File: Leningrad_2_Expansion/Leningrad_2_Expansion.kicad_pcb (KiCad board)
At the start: 2 copper layers, 40 x 71 mm, 2 parts, among them J1 ZX_Spectrum_Connector_48K, X6 Leningrad 2 Expansion Bus

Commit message: PCB changes
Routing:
- net GND: track 136.5 -> 119.8 mm, vias 24 -> 32
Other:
- board text added: "28A"
- board text added: "4A"
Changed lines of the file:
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@@
+		)
+	)
+	(gr_text "4A"
+		(at 77.599998 31.878654 0)
+		(layer "F.SilkS")
+		(effects
+			(font
+				(size 1 1)
+				(thickness 0.1)
+			)
+			(justify left bottom)
 		)
 	)
@@
 		)
 	)
+	(gr_text "28A"
+		(at 77.599998 92.578654 0)
+		(layer "F.SilkS")
+		(effects
+			(font
+				(size 1 1)
+				(thickness 0.1)
+			)
+			(justify left bottom)
+		)
+	)
 	(gr_text "21A (~{WAIT})"
 		(at 77.599998 75.057308 0)
@@
 		(layer "B.Cu")
 		(net 14)
-	)
-	(segment
-		(start 76.849998 62.007308)
-		(end 78.799998 63.957308)
-		(width 0.5)
-		(layer "F.Cu")
-		(net 15)
 	)
 	(segment
@@
 	)
 	(segment
-		(start 73.799998 50.74073)
-		(end 73.799998 51.457308)
+		(start 66.199999 48.178654)
+		(end 66.599999 48.578654)
 		(width 0.5)
 		(layer "F.Cu")
@@
 	)
 	(segment
-		(start 78.38342 46.157308)
-		(end 73.799998 50.74073)
-		(width 0.5)
-		(layer "F.Cu")
-		(net 15)
-	)
-	(segment
-		(start 65.099998 68.057308)
-		(end 65.099998 65.657308)
-		(width 0.5)
-		(layer "F.Cu")
-		(net 15)
-	)
-	(segment
-		(start 80.399998 49.857308)
-		(end 85.299998 49.857308)
-		(width 0.5)
-		(layer "F.Cu")
-		(net 15)
-	)
-	(segment
 		(start 78.099998 71.257308)
 		(end 80.099998 73.257308)
@@
 	)
 	(segment
-		(start 85.299998 49.857308)
-		(end 85.399998 49.957308)
-		(width 0.5)
-		(layer "F.Cu")
-		(net 15)
-	)
-	(segment
-		(start 80.499998 46.157308)
-		(end 78.38342 46.157308)
-		(width 0.5)
-		(layer "F.Cu")
-		(net 15)
-	)
-	(segment
-		(start 75.299998 60.457308)
-		(end 76.849998 62.007308)
-		(width 0.5)
-		(layer "F.Cu")
-		(net 15)
-	)
-	(segment
-		(start 78.799998 63.957308)
-		(end 80.499998 63.957308)
+		(start 60.099999 48.178654)
+		(end 66.199999 48.178654)
 		(width 0.5)
 		(layer "F.Cu")
@@
 	)
 	(via
+		(at 56.299999 23.978654)
+		(size 0.6)
+		(drill 0.3)
+		(layers "F.Cu" "B.Cu")
+		(free yes)
+		(net 15)
+	)
+	(via
+		(at 73.099999 45.278654)
+		(size 0.6)
+		(drill 0.3)
+		(layers "F.Cu" "B.Cu")
+		(free yes)
+		(net 15)
+	)
+	(via
 		(at 83.899998 78.157308)
 		(size 0.6)
@@
 	)
 	(via
+		(at 75.299999 64.878654)
+		(size 0.6)
+		(drill 0.3)
+		(layers "F.Cu" "B.Cu")
+		(free yes)
+		(net 15)
+	)
+	(via
 		(at 68.199998 80.757308)
 		(size 0.6)
@@
 	)
 	(via
+		(at 64.099999 60.878654)
+		(size 0.6)
+		(drill 0.3)
+		(layers "F.Cu" "B.Cu")
+		(free yes)
+		(net 15)
+	)
+	(via
 		(at 75.299998 60.457308)
 		(size 0.6)
@@
 	)
 	(via
+		(at 66.599999 48.578654)
+		(size 0.6)
+		(drill 0.3)
+		(layers "F.Cu" "B.Cu")
+		(net 15)
+	)
+	(via
 		(at 73.799998 51.457308)
 		(size 0.6)
@@
 	)
 	(via
+		(at 66.699999 44.278654)
+		(size 0.6)
+		(drill 0.3)
+		(layers "F.Cu" "B.Cu")
+		(free yes)
+		(net 15)
+	)
+	(via
+		(at 68.899999 53.878654)
+		(size 0.6)
+		(drill 0.3)
+		(layers "F.Cu" "B.Cu")
+		(free yes)
+		(net 15)
+	)
+	(via
 		(at 80.499998 63.957308)
 		(size 0.6)
@@
 		(net 15)
 	)
+	(via
+		(at 66.499999 39.978654)
+		(size 0.6)
+		(drill 0.3)
+		(layers "F.Cu" "B.Cu")
+		(free yes)
+		(net 15)
+	)

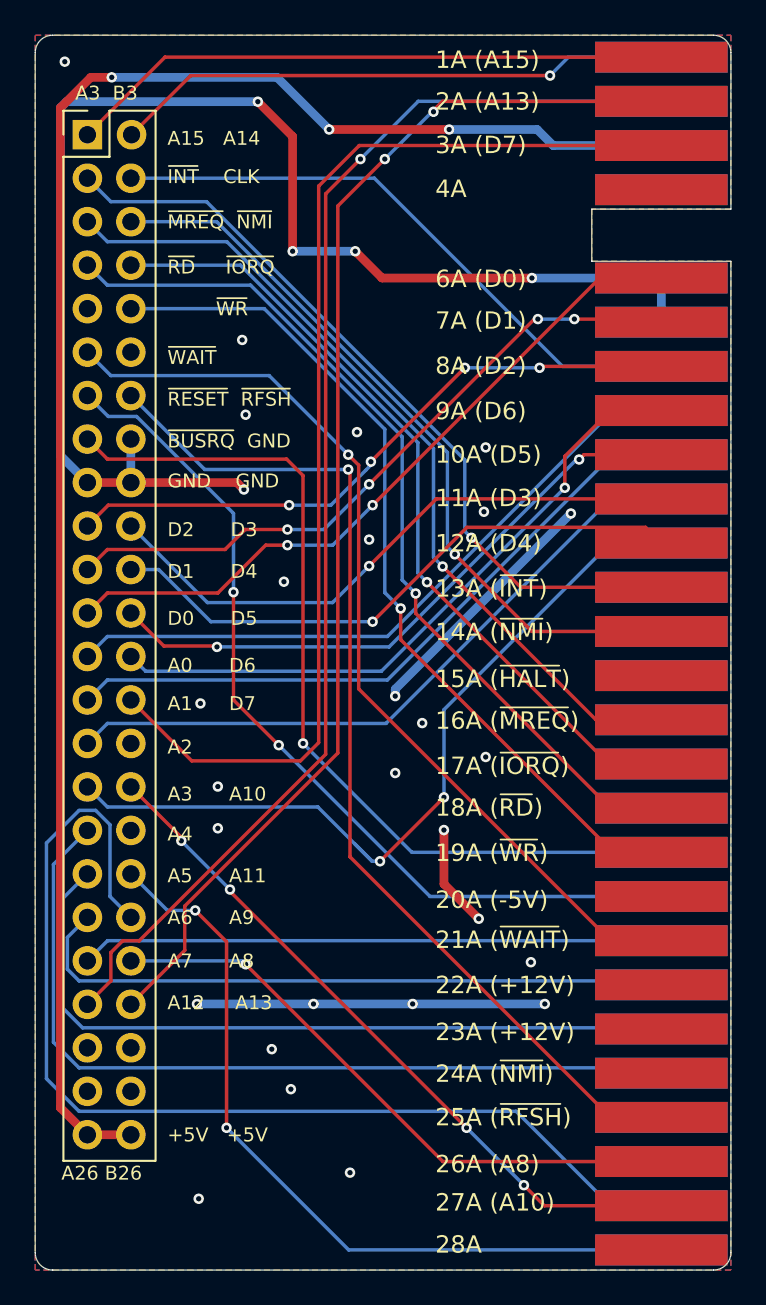
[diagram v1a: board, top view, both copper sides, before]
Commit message: Added ~IORQGE signal
Thanks to Oleh S. suggestion on UCHC "Ukrainian Computing History Community"
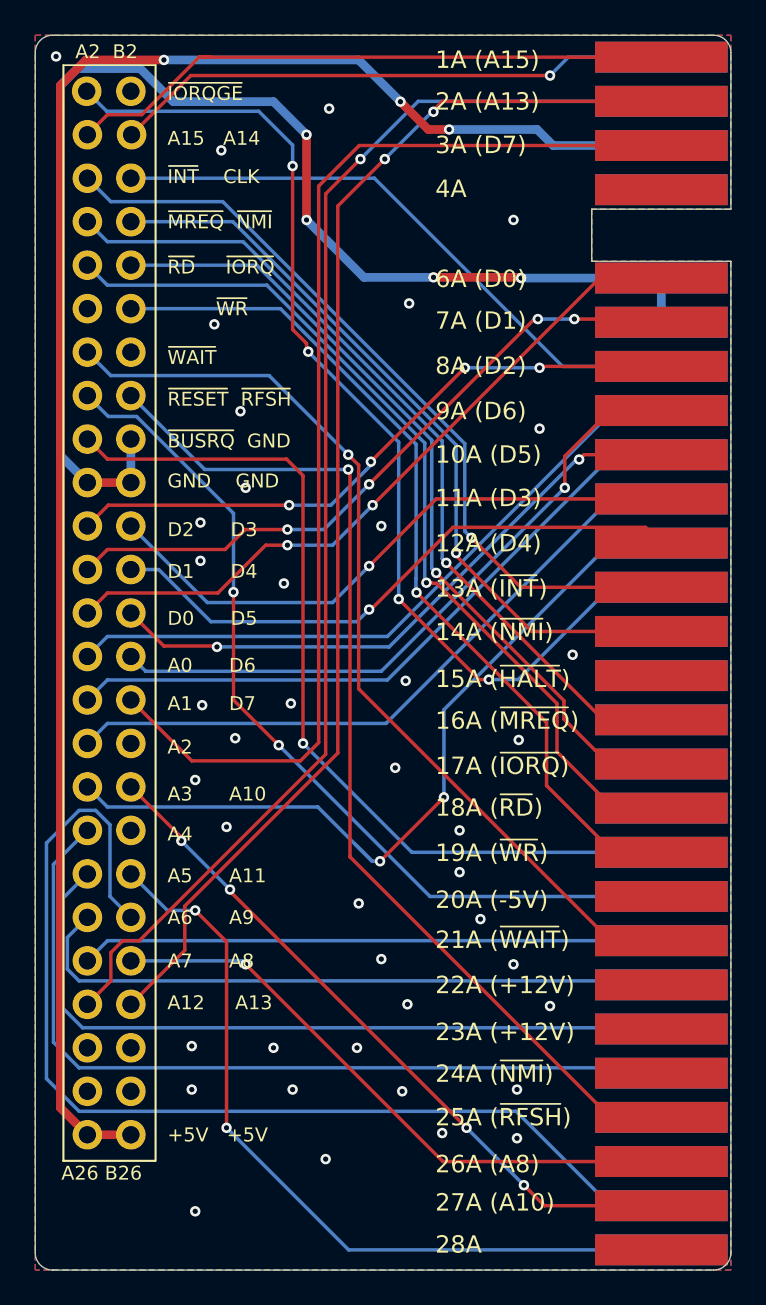
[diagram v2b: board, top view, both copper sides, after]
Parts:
- X6: value Leningrad 2 Expansion Bus -> Ленинград-2 Expansion Bus
- moved X6 2.00 mm to (58.8, 20.0)
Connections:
- J1 pad A13: unconnected-(J1-IORQGE-PadA13) -> /~{IORQGE}
- X6 pad A14: /D5 -> unconnected-(X6-D5-PadA14)
- X6 pad A15: /D6 -> unconnected-(X6-D6-PadA15)
- X6 pad A16: /D7 -> unconnected-(X6-D7-PadA16)
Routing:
- net /~{IORQGE}: track 0.00 -> 61.1 mm, vias 0 -> 4
- net GND: track 119.8 -> 73.8 mm, vias 32 -> 45
- net /~{RD}: track 51.4 -> 55.1 mm
- net +5V: track 99.1 -> 100.7 mm
- net /A15: track 34.8 -> 35.5 mm
- net /~{WR}: track 52.9 -> 53.5 mm
- net /~{NMI}: track 43.4 -> 44.0 mm
- net /~{IORQ}: track 46.8 -> 47.3 mm
- net /~{INT}: track 45.1 -> 45.7 mm
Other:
- board text added: "A2 B2"
- board text added: "~{IORQGE}"
- board text added: "Ленинград-2 To ZX Spectrum (Rev. B) Brett Hallen, Nov 2025 www.youtube.com/@Brfff Note: Ленинград-2 is 2.5mm pitch"
- board text removed: "A3 B3"
- board text removed: "Ленинград-2 To ZX Spectrum (Rev. A) Brett Hallen, Nov 2025 www.youtube.com/@Brfff Note: Ленинград-2 is 2.5mm pitch"

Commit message: Update Leningrad_2_Expansion.kicad_pcb
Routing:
- net /~{BUSRQ}: track 51.9 -> 52.9 mm
- net GND: vias 45 -> 48
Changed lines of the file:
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@@
+	)
+	(segment
+		(start 60.099999 45.678654)
+		(end 60.099999 48.178654)
+		(width 0.5)
+		(layer "F.Cu")
+		(net 15)
 	)
 	(segment
@@
 	)
 	(via
+		(at 66.799999 31.778654)
+		(size 0.6)
+		(drill 0.3)
+		(layers "F.Cu" "B.Cu")
+		(free yes)
+		(net 15)
+	)
+	(via
 		(at 82.099999 33.078654)
 		(size 0.6)
@@
 	)
 	(via
-		(at 64.199999 60.978654)
+		(at 63.899999 60.778654)
 		(size 0.6)
 		(drill 0.3)
@@
 	)
 	(via
-		(at 64.099999 52.678654)
+		(at 64.099999 53.178654)
 		(size 0.6)
 		(drill 0.3)
@@
 	)
 	(via
+		(at 74.599999 56.078654)
+		(size 0.6)
+		(drill 0.3)
+		(layers "F.Cu" "B.Cu")
+		(free yes)
+		(net 15)
+	)
+	(via
 		(at 82.299999 83.078654)
 		(size 0.6)
@@
 	)
 	(via
-		(at 66.399999 44.078654)
+		(at 66.399999 43.578654)
 		(size 0.6)
 		(drill 0.3)
@@
 	)
 	(via
-		(at 69.299999 60.878654)
+		(at 69.099999 60.878654)
 		(size 0.6)
 		(drill 0.3)
@@
 		(drill 0.3)
 		(layers "F.Cu" "B.Cu")
+		(net 15)
+	)
+	(via
+		(at 74.099999 58.278654)
+		(size 0.6)
+		(drill 0.3)
+		(layers "F.Cu" "B.Cu")
+		(free yes)
 		(net 15)
 	)
@@
 	)
 	(segment
-		(start 60.099999 48.178654)
-		(end 60.099999 45.678654)
-		(width 0.5)
-		(layer "B.Cu")
-		(net 15)
-	)
-	(segment
 		(start 60.638891 24.377654)
 		(end 57.021107 24.377654)
@@
 	)
 	(segment
+		(start 58.799999 44.478654)
+		(end 57.599999 45.678654)
+		(width 0.2)
+		(layer "F.Cu")
+		(net 34)
+	)
+	(segment
 		(start 69.999999 63.178654)
 		(end 69.999999 47.778654)
@@
 	)
 	(segment
-		(start 69.050999 46.829654)
-		(end 58.750999 46.829654)
+		(start 69.999999 47.778654)
+		(end 66.699999 44.478654)
 		(width 0.2)
 		(layer "F.Cu")
@@
 	)
 	(segment
-		(start 69.999999 47.778654)
-		(end 69.050999 46.829654)
-		(width 0.2)
-		(layer "F.Cu")
-		(net 34)
-	)
-	(segment
-		(start 58.750999 46.829654)
-		(end 57.599999 45.678654)
-		(width 0.2)
-		(layer "F.Cu")
+		(start 66.699999 44.478654)
+		(end 58.799999 44.478654)
+		(width 0.2)
+		(layer "F.Cu")

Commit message: PCB updates
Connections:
- X6 pad A14: unconnected-(X6-D5-PadA14) -> /D5
- X6 pad A15: unconnected-(X6-D6-PadA15) -> /D6
- X6 pad A16: unconnected-(X6-D7-PadA16) -> /D7
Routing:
- net /A3: track 46.7 -> 45.3 mm
- net /A15: track 35.5 -> 34.8 mm
- net GND: vias 48 -> 47
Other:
- board text added: "+5V"
- board text added: "A0"
- board text added: "A1"
- board text added: "A10"
- board text added: "A11"
- board text added: "A12"
- board text added: "A13"
- board text added: "A14"
- board text added: "A15"
- board text added: "A3"
- board text added: "A5"
- board text added: "A6"
- board text added: "A7"
- board text added: "A8"
- board text added: "A9"
- board text added: "CLK"
- board text added: "D0"
- board text added: "D1"
- board text added: "D2"
- board text added: "D3"
- board text added: "D4"
- board text added: "D5"
- board text added: "D6"
- board text added: "D7"
- board text added: "GND"
- board text added: "~{BUSRQ}"
- board text added: "~{INT}"
- board text added: "~{IORQ}"
- board text added: "~{MREQ}"
- board text added: "~{NMI}"
- board text added: "~{RD}"
- board text added: "~{RESET}"
- board text added: "~{RFSH}"
- board text removed: "+5V +5V"
- board text removed: "A0 D6"
- board text removed: "A1 D7"
- board text removed: "A12 A13"
- board text removed: "A15 A14"
- board text removed: "A3 A10"
- board text removed: "A5 A11"
- board text removed: "A6 A9"
- board text removed: "A7 A8"
- board text removed: "D0 D5"
- board text removed: "D1 D4"
- board text removed: "D2 D3"
- board text removed: "GND GND"
- board text removed: "~{BUSRQ} GND"
- board text removed: "~{INT} CLK"
- board text removed: "~{MREQ} ~{NMI}"
- board text removed: "~{RD} ~{IORQ}"
- board text removed: "~{RESET} ~{RFSH}"
